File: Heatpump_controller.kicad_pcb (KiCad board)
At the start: 2 copper layers, 76 parts, among them J1 Conn_01x03, J2 USB_C_Receptacle_USB2.0_16P, J3 Conn_01x03, J4 Conn_01x03, J5 RJ12, J6 RJ12, J7 RJ45_Hanrun_HR911105A_Horizon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, K1 SANYOU_SRD_Form_C, K2 SANYOU_SRD_Form_C, K3 SANYOU_SRD_Form_C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

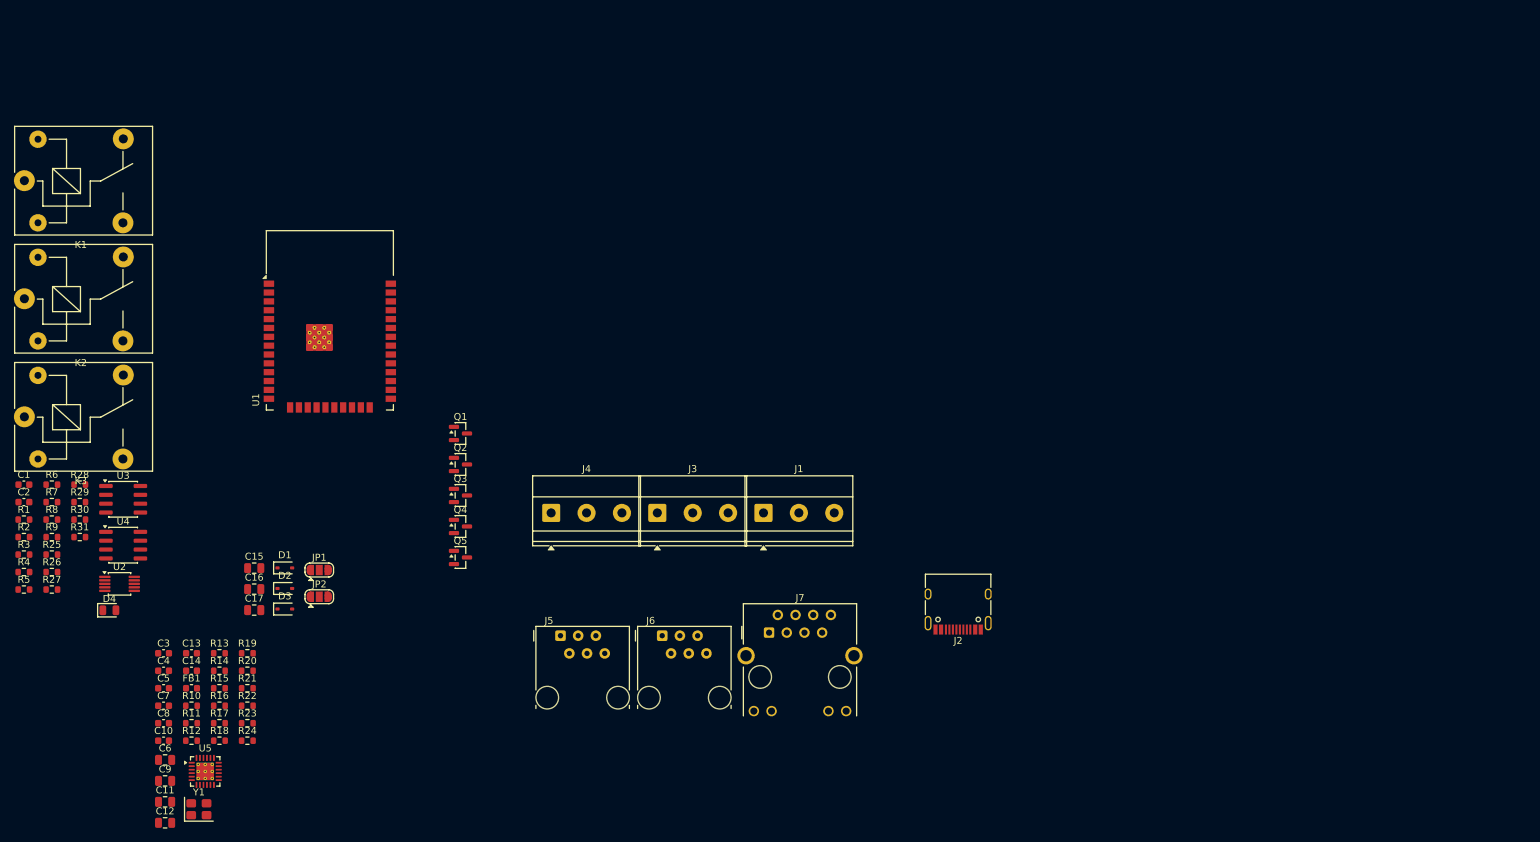
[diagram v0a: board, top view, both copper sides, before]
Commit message: Added PCB outline
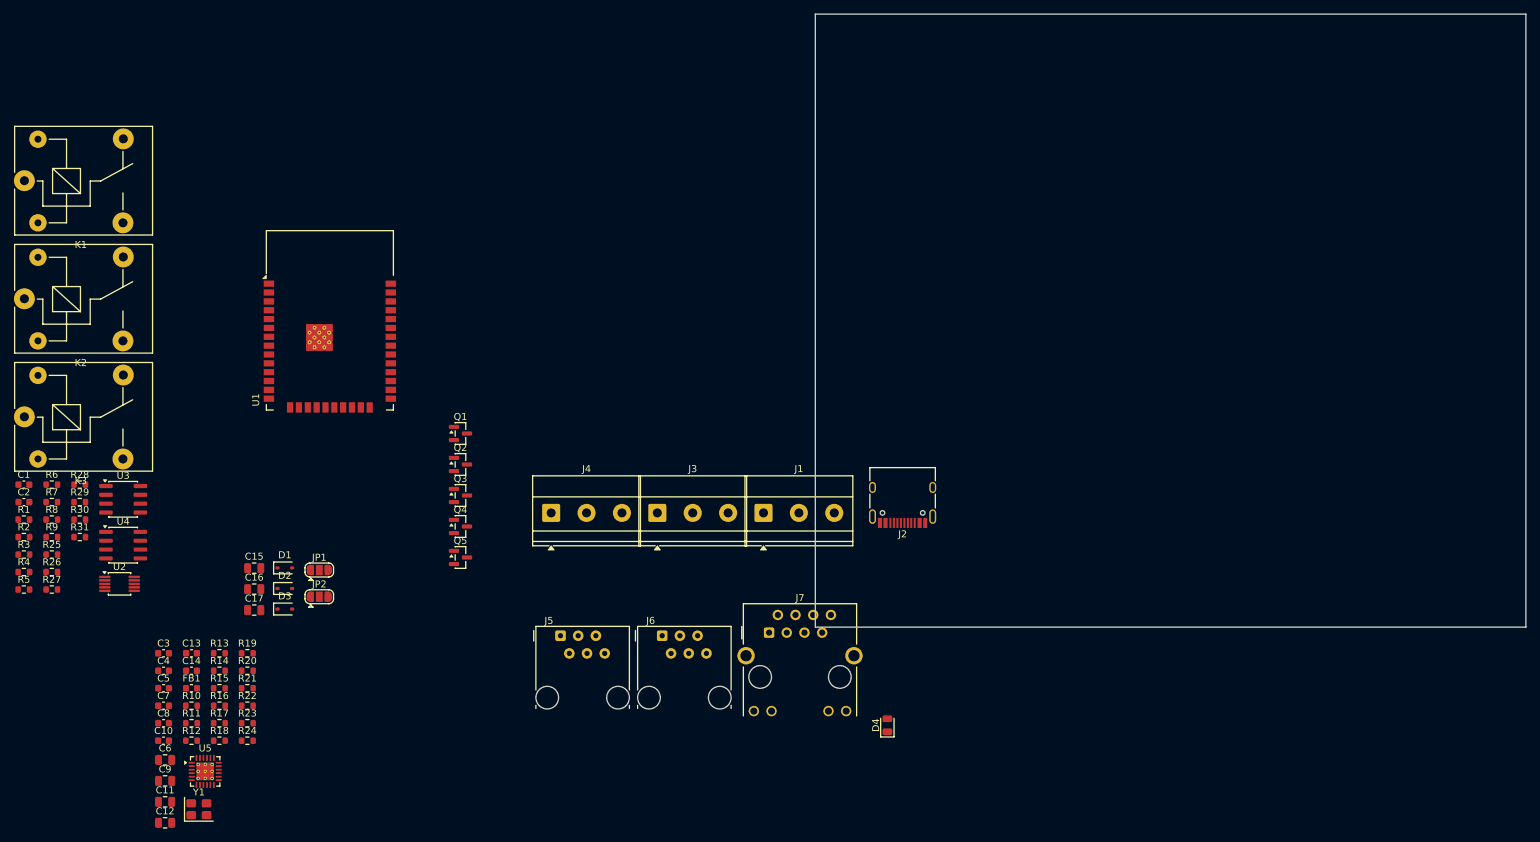
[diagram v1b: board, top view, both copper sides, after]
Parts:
- moved D4 112.9 mm to (180.3, 132.1), turned to 90 degrees
- moved J2 17.3 mm to (182.5, 99.0)
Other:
- board outline added: 102 x 88 mm
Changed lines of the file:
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@@
 	(footprint "LED_SMD:LED_0805_2012Metric"
 		(layer "F.Cu")
-		(at 68.6625 115.575)
+		(at 180.34 132.08 90)
 		(descr "LED SMD 0805 (2012 Metric), square (rectangular) end terminal, IPC-7351 nominal, (Body size source: https://docs.google.com/spreadsheets/d/1BsfQQcO9C6DZCsRaXUlFlo91Tg2WpOkGARC1WS5S8t0/edit?usp=sharing), generated with kicad-footprint-generator")
 		(tags "LED")
 		(property "Reference" "D4"
-			(at 0 -1.65 0)
+			(at 0 -1.65 90)
 			(layer "F.SilkS")
 			(effects
@@
 		)
 		(property "Value" "LED"
-			(at 0 1.65 0)
+			(at 0 1.65 90)
 			(layer "F.Fab")
 			(effects
@@
 		)
 		(property "Datasheet" "~"
-			(at 0 0 0)
+			(at 0 0 90)
 			(layer "F.Fab")
 			(hide yes)
@@
 		)
 		(property "Description" "Light emitting diode"
-			(at 0 0 0)
+			(at 0 0 90)
 			(layer "F.Fab")
 			(hide yes)
@@
 		)
 		(property "Sim.Pins" "1=K 2=A"
-			(at 0 0 0)
+			(at 0 0 90)
 			(unlocked yes)
 			(layer "F.Fab")
@@
 		(attr smd)
 		(fp_line
-			(start -1.685 -0.96)
-			(end -1.685 0.96)
+			(start 1 -0.96)
+			(end -1.685 -0.96)
 			(stroke
 				(width 0.12)
@@
 		)
 		(fp_line
-			(start -1.685 0.96)
-			(end 1 0.96)
+			(start -1.685 -0.96)
+			(end -1.685 0.96)
 			(stroke
 				(width 0.12)
@@
 		)
 		(fp_line
-			(start 1 -0.96)
-			(end -1.685 -0.96)
+			(start -1.685 0.96)
+			(end 1 0.96)
 			(stroke
 				(width 0.12)
@@
 		)
 		(fp_line
-			(start -1.68 -0.95)
-			(end 1.68 -0.95)
+			(start 1.68 -0.95)
+			(end 1.68 0.95)
 			(stroke
 				(width 0.05)
@@
 		)
 		(fp_line
-			(start -1.68 0.95)
-			(end -1.68 -0.95)
+			(start -1.68 -0.95)
+			(end 1.68 -0.95)
 			(stroke
 				(width 0.05)
@@
 		)
 		(fp_line
-			(start 1.68 -0.95)
-			(end 1.68 0.95)
+			(start 1.68 0.95)
+			(end -1.68 0.95)
 			(stroke
 				(width 0.05)
@@
 		)
 		(fp_line
-			(start 1.68 0.95)
-			(end -1.68 0.95)
+			(start -1.68 0.95)
+			(end -1.68 -0.95)
 			(stroke
 				(width 0.05)
@@
 		)
 		(fp_line
-			(start -1 -0.3)
-			(end -1 0.6)
+			(start 1 -0.6)
+			(end -0.7 -0.6)
 			(stroke
 				(width 0.1)
@@
 		)
 		(fp_line
-			(start -1 0.6)
-			(end 1 0.6)
+			(start -0.7 -0.6)
+			(end -1 -0.3)
 			(stroke
 				(width 0.1)
@@
 		)
 		(fp_line
-			(start -0.7 -0.6)
-			(end -1 -0.3)
+			(start -1 -0.3)
+			(end -1 0.6)
 			(stroke
 				(width 0.1)
@@
 		)
 		(fp_line
-			(start 1 -0.6)
-			(end -0.7 -0.6)
+			(start 1 0.6)
+			(end 1 -0.6)
 			(stroke
 				(width 0.1)
@@
 		)
 		(fp_line
-			(start 1 0.6)
-			(end 1 -0.6)
+			(start -1 0.6)
+			(end 1 0.6)
 			(stroke
 				(width 0.1)
@@
 		)
 		(fp_text user "${REFERENCE}"
-			(at 0 0 0)
+			(at 0 0 90)
 			(layer "F.Fab")
 			(effects
@@
 		)
 		(pad "1" smd roundrect
-			(at -0.9375 0)
+			(at -0.9375 0 90)
 			(size 0.975 1.4)
 			(layers "F.Cu" "F.Mask" "F.Paste")
@@
 		)
 		(pad "2" smd roundrect
-			(at 0.9375 0)
+			(at 0.9375 0 90)
 			(size 0.975 1.4)
 			(layers "F.Cu" "F.Mask" "F.Paste")
@@
 	(footprint "Connector_USB:USB_C_Receptacle_HRO_TYPE-C-31-M-12"
 		(layer "F.Cu")
-		(at 190.5 114.3 180)
+		(at 182.53 99 180)
 		(descr "USB Type-C receptacle for USB 2.0 and PD, http://www.krhro.com/uploads/soft/180320/1-1P320120243.pdf")
 		(tags "usb usb-c 2.0 pd")
@@
 		)
 	)
+	(gr_rect
+		(start 170 30)
+		(end 272 118)
+		(stroke
+			(width 0.05)
+			(type default)
+		)
+		(fill no)
+		(layer "Edge.Cuts")
+	)
 	(embedded_fonts no)

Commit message: Finished route
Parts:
- added C18: 10uF, Capacitor_SMD:C_0805_2012Metric, F.Cu at (189.2, 72.0)
- added C19: 10uF, Capacitor_SMD:C_0805_2012Metric, F.Cu at (189.2, 70.0)
- added C20: 8.2nF, Capacitor_SMD:C_0603_1608Metric, F.Cu at (182.8, 71.2)
- added C21: 10pF, Capacitor_SMD:C_0603_1608Metric, F.Cu at (185.6, 81.5)
- added C22: 5.6nF, Capacitor_SMD:C_0603_1608Metric, F.Cu at (185.6, 86.3)
- added C23: 100nF, Capacitor_SMD:C_0603_1608Metric, F.Cu at (189.3, 80.3)
- added C24: 47uF, Capacitor_SMD:C_0805_2012Metric, F.Cu at (195.8, 78.3)
- added C25: 100nF, Capacitor_SMD:C_0603_1608Metric, F.Cu at (199.4, 101.3)
- added C26: 100nF, Capacitor_SMD:C_0603_1608Metric, F.Cu at (194.2, 101.3)
- added D5: SS34, Diode_SMD:D_SMA, F.Cu at (191.9, 76.5)
- added H1: MountingHole, MountingHole:MountingHole_3.2mm_M3, F.Cu at (182.8, 34.0)
- added H2: MountingHole, MountingHole:MountingHole_3.2mm_M3, F.Cu at (267.8, 34.0)
- added H3: MountingHole, MountingHole:MountingHole_3.2mm_M3, F.Cu at (182.8, 114.0)
- added H4: MountingHole, MountingHole:MountingHole_3.2mm_M3, F.Cu at (267.8, 114.0)
- added L1: 15uH, Inductor_SMD:L_Changjiang_FXL0630, F.Cu at (193.8, 84.0)
- added R32: 5.62k, Resistor_SMD:R_0603_1608Metric, F.Cu at (184.8, 84.0)
- added R33: 10.2k, Resistor_SMD:R_0603_1608Metric, F.Cu at (183.2, 88.8)
- added R34: 3.24k, Resistor_SMD:R_0603_1608Metric, F.Cu at (185.6, 88.0)
- added U6: TPS54331, Package_SO:SOIC-8_3.9x4.9mm_P1.27mm, F.Cu at (185.6, 76.8)
- moved R30 199.4 mm to (260.8, 68.1), turned to -90 degrees
- moved C2 199.0 mm to (255.4, 97.0), turned to 180 degrees
- moved R9 193.7 mm to (254.0, 98.6)
- moved R8 190.6 mm to (251.0, 98.6)
- moved R1 189.2 mm to (242.5, 68.3), turned to 90 degrees
- moved R7 187.6 mm to (248.0, 98.6)
- moved K1 185.9 mm to (242.2, 47.0), turned to -90 degrees
- moved C1 184.0 mm to (240.4, 97.0), turned to 180 degrees
- moved U4 180.8 mm to (251.0, 94.0), turned to -90 degrees
- moved R4 180.0 mm to (236.0, 98.6)
- moved R29 179.8 mm to (243.8, 87.2), turned to 180 degrees
- moved C16 179.7 mm to (263.4, 67.4)
- moved C15 179.5 mm to (263.4, 65.4)
- moved R6 178.6 mm to (239.0, 98.6)
- moved R5 177.2 mm to (233.0, 98.6)
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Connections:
- net Net-(J7-RD+) renamed /Ethernet/RX_P
- net Net-(J7-RD-) renamed /Ethernet/RX_N
- net Net-(J7-TD+) renamed /Ethernet/TX_P
- net Net-(J7-TD-) renamed /Ethernet/TX_N
- R24 pad 2: /MDC -> /MDIO
- U1 pad 24: Net-(Q1-G) -> Net-(Q2-G)
- U1 pad 26: Net-(Q2-G) -> Net-(Q3-G)
- U1 pad 8: Net-(Q3-G) -> Net-(Q1-G)
- U5 pad 12: /MDC -> /MDIO
- U5 pad 13: /MDIO -> /MDC
- Y1 pad 2: unconnected-(Y1-Pad2) -> GND
- Y1 pad 4: unconnected-(Y1-Pad4) -> GND
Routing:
- net Net-(D4-A): track 0.00 -> 109.3 mm, vias 0 -> 2
- net /UART_TX: track 0.00 -> 101.6 mm, vias 0 -> 2
- net /UART_RX: track 0.00 -> 100.9 mm, vias 0 -> 2
- net /RST: track 0.00 -> 100.6 mm, vias 0 -> 2
- net GND: track 0.00 -> 83.2 mm, vias 0 -> 66
- net /GPIO0: track 0.00 -> 76.7 mm, vias 0 -> 2
- net Net-(Q3-G): track 0.00 -> 65.2 mm
- net /MDC: track 0.00 -> 57.9 mm, vias 0 -> 2
- net /TXD1: track 0.00 -> 54.3 mm, vias 0 -> 2
- net /CRS_DV: track 0.00 -> 53.8 mm, vias 0 -> 2
- net /TX_EN: track 0.00 -> 53.3 mm, vias 0 -> 2
- net /RST_ETH: track 0.00 -> 52.7 mm, vias 0 -> 2
- net /MDIO: track 0.00 -> 51.5 mm, vias 0 -> 2
- net +3.3V: track 0.00 -> 51.4 mm, vias 0 -> 23
- net +5V: track 0.00 -> 50.7 mm, vias 0 -> 6
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- added copper zone on F.Cu, net +3.3V
- added copper zone on In2.Cu, net +3.3V
- added copper zone on F.Cu, net +5V
- added copper zone on In2.Cu, net +5V
- added copper zone on F.Cu, net GND
- added copper zone on In1.Cu, net GND
- added copper zone on F.Cu, net Net-(D5-K)
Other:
- board size 102 x 88 mm -> 93.5 x 88 mm
- copper layers 2 -> 4
